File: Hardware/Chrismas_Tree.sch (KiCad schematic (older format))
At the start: 0 parts

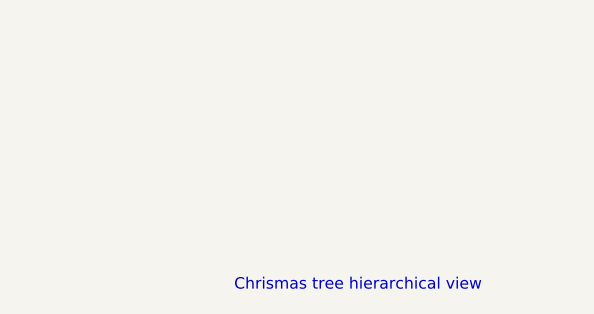
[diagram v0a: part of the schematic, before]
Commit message: Used standard schematic title blocks titles.
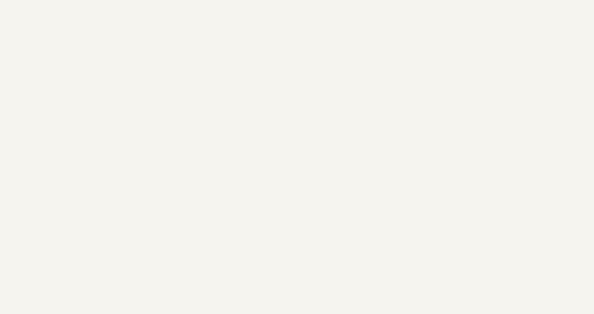
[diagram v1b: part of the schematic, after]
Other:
- note removed: "Chrismas tree hierarchical view"
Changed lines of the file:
@@
 EESchema Schematic File Version 4
-LIBS:Chrismas_Tree-cache
 EELAYER 30 0
 EELAYER END
@@
 encoding utf-8
 Sheet 1 3
-Title ""
+Title "Chrismas tree hierarchical view"
 Date ""
 Rev ""
-Comp ""
+Comp "Adrien RICCIARDI"
 Comment1 ""
 Comment2 ""
@@
 F1 "Tree_Shape.sch" 50
 $EndSheet
-Text Notes 7400 7500 0    50   ~ 0
-Chrismas tree hierarchical view
 $Sheet
 S 4600 3350 1250 1100

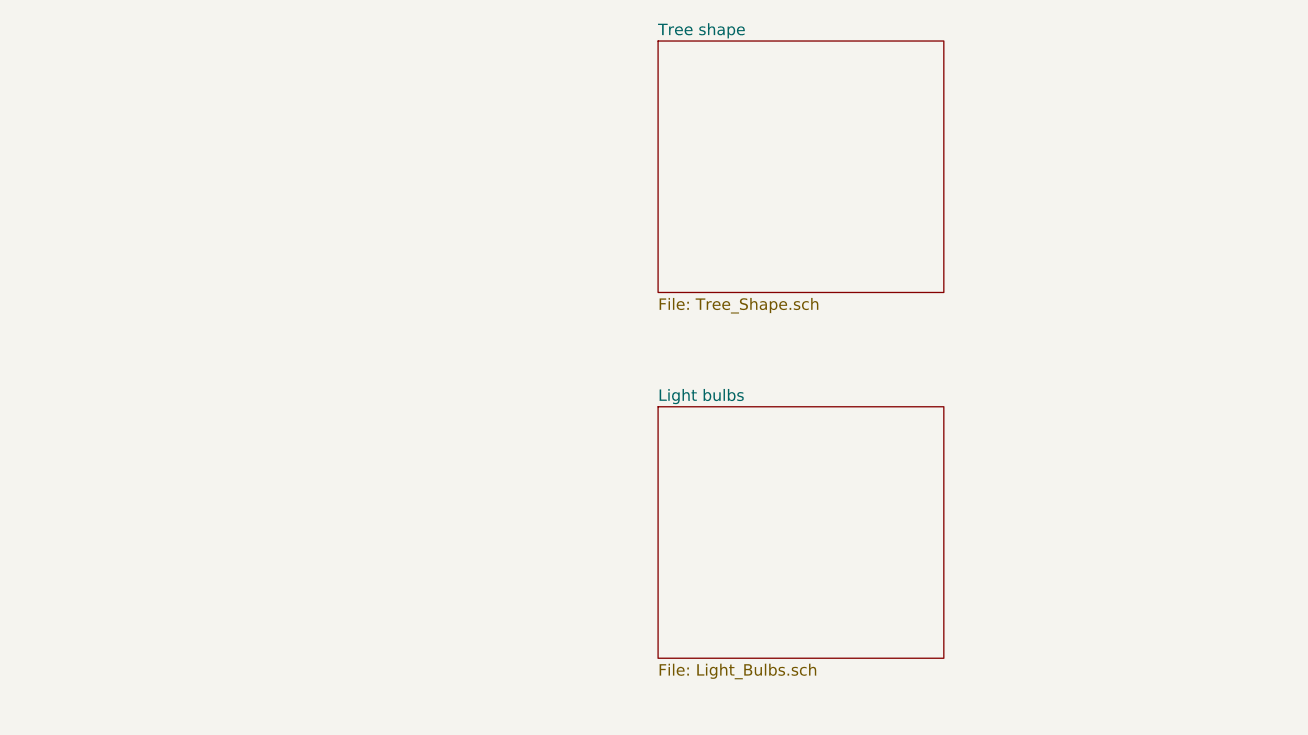
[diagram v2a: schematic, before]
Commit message: Added mounting holes to schematic.
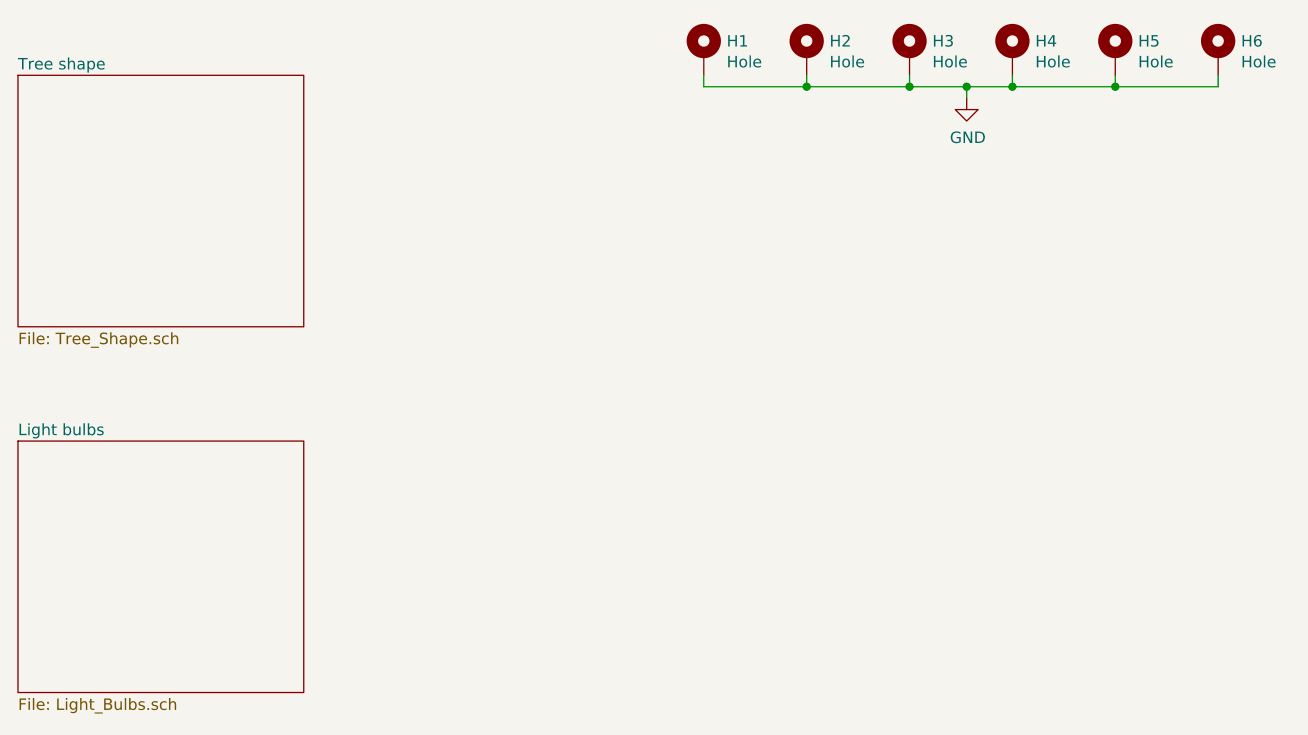
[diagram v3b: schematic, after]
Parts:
- added H1, H2, H3, H4, H5, H6: Hole, MountingHole:MountingHole_4.5mm_Pad, symbol Mechanical:MountingHole_Pad
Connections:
- new net GND: H1.1, H2.1, H3.1, H4.1, H5.1, H6.1
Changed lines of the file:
@@
 $EndDescr
 $Sheet
-S 4600 1750 1250 1100
+S 1800 1900 1250 1100
 U 5DE1DFF6
 F0 "Tree shape" 50
@@
 $EndSheet
 $Sheet
-S 4600 3350 1250 1100
+S 1800 3500 1250 1100
 U 5DE2A82E
 F0 "Light bulbs" 50
 F1 "Light_Bulbs.sch" 50
 $EndSheet
+$Comp
+L Mechanical:MountingHole_Pad H1
+U 1 1 5DE4B967
+P 4800 1800
+F 0 "H1" H 4900 1849 50  0000 L CNN
+F 1 "Hole" H 4900 1758 50  0000 L CNN
+F 2 "MountingHole:MountingHole_4.5mm_Pad" H 4800 1800 50  0001 C CNN
+F 3 "~" H 4800 1800 50  0001 C CNN
+	1    4800 1800
+	1    0    0    -1
+$EndComp
+$Comp
+L Mechanical:MountingHole_Pad H2
+U 1 1 5DE4DC82
+P 5250 1800
+F 0 "H2" H 5350 1849 50  0000 L CNN
+F 1 "Hole" H 5350 1758 50  0000 L CNN
+F 2 "MountingHole:MountingHole_4.5mm_Pad" H 5250 1800 50  0001 C CNN
+F 3 "~" H 5250 1800 50  0001 C CNN
+	1    5250 1800
+	1    0    0    -1
+$EndComp
+$Comp
+L Mechanical:MountingHole_Pad H3
+U 1 1 5DE4DF24
+P 5700 1800
+F 0 "H3" H 5800 1849 50  0000 L CNN
+F 1 "Hole" H 5800 1758 50  0000 L CNN
+F 2 "MountingHole:MountingHole_4.5mm_Pad" H 5700 1800 50  0001 C CNN
+F 3 "~" H 5700 1800 50  0001 C CNN
+	1    5700 1800
+	1    0    0    -1
+$EndComp
+$Comp
+L Mechanical:MountingHole_Pad H4
+U 1 1 5DE4E445
+P 6150 1800
+F 0 "H4" H 6250 1849 50  0000 L CNN
+F 1 "Hole" H 6250 1758 50  0000 L CNN
+F 2 "MountingHole:MountingHole_4.5mm_Pad" H 6150 1800 50  0001 C CNN
+F 3 "~" H 6150 1800 50  0001 C CNN
+	1    6150 1800
+	1    0    0    -1
+$EndComp
+$Comp
+L Mechanical:MountingHole_Pad H5
+U 1 1 5DE4E44F
+P 6600 1800
+F 0 "H5" H 6700 1849 50  0000 L CNN
+F 1 "Hole" H 6700 1758 50  0000 L CNN
+F 2 "MountingHole:MountingHole_4.5mm_Pad" H 6600 1800 50  0001 C CNN
+F 3 "~" H 6600 1800 50  0001 C CNN
+	1    6600 1800
+	1    0    0    -1
+$EndComp
+$Comp
+L Mechanical:MountingHole_Pad H6
+U 1 1 5DE4E459
+P 7050 1800
+F 0 "H6" H 7150 1849 50  0000 L CNN
+F 1 "Hole" H 7150 1758 50  0000 L CNN
+F 2 "MountingHole:MountingHole_4.5mm_Pad" H 7050 1800 50  0001 C CNN
+F 3 "~" H 7050 1800 50  0001 C CNN
+	1    7050 1800
+	1    0    0    -1
+$EndComp
+$Comp
+L power:GND #PWR0102
+U 1 1 5DE4EE07
+P 5950 2000
+F 0 "#PWR0102" H 5950 1750 50  0001 C CNN
+F 1 "GND" H 5955 1827 50  0000 C CNN
+F 2 "" H 5950 2000 50  0001 C CNN
+F 3 "" H 5950 2000 50  0001 C CNN
+	1    5950 2000
+	1    0    0    -1
+$EndComp
+Wire Wire Line
+	4800 1900 4800 1950
+Wire Wire Line
+	4800 1950 5250 1950
+Wire Wire Line
+	5250 1950 5250 1900
+Wire Wire Line
+	5250 1950 5700 1950
+Wire Wire Line
+	5700 1950 5700 1900
+Connection ~ 5250 1950
+Wire Wire Line
+	5700 1950 5950 1950
+Wire Wire Line
+	6150 1950 6150 1900
+Connection ~ 5700 1950
+Wire Wire Line
+	5950 1950 5950 2000
+Connection ~ 5950 1950
+Wire Wire Line
+	5950 1950 6150 1950
+Wire Wire Line
+	6150 1950 6600 1950
+Wire Wire Line
+	6600 1950 6600 1900
+Connection ~ 6150 1950
+Wire Wire Line
+	6600 1950 7050 1950
+Wire Wire Line
+	7050 1950 7050 1900
+Connection ~ 6600 1950
 $EndSCHEMATC

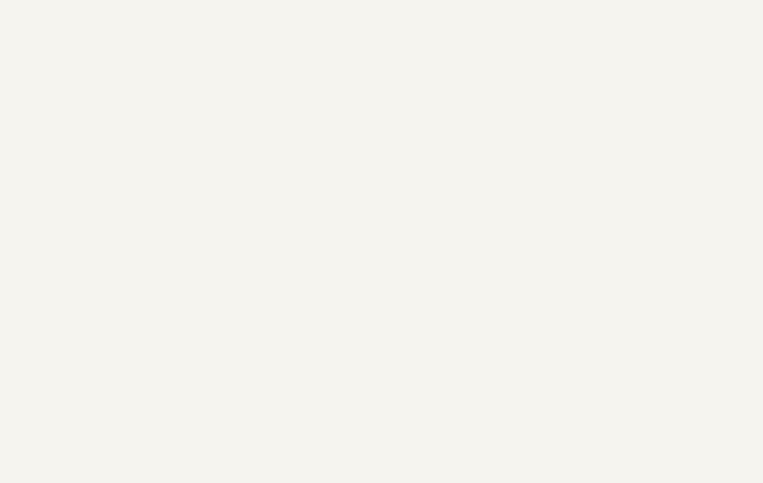
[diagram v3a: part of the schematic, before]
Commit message: Replaced USB micro B connector by a more robust USB B one.
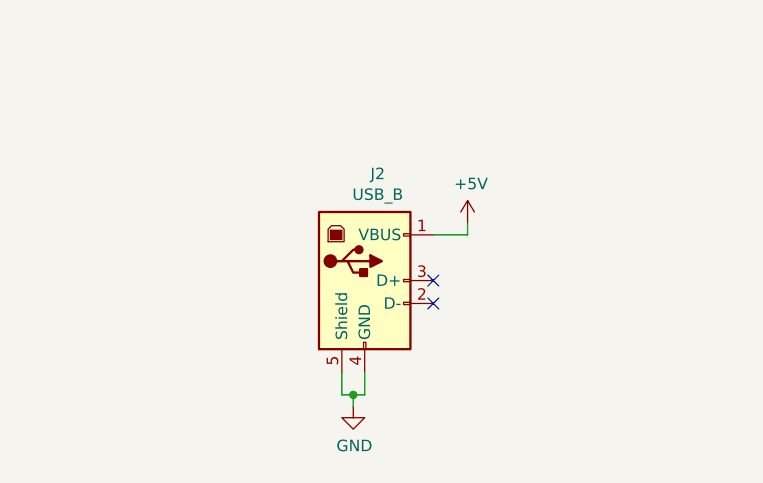
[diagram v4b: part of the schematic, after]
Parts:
- added J2: USB_B, Connector_USB:USB_B_OST_USB-B1HSxx_Horizontal, symbol Connector:USB_B
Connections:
- net GND: now also J2.4 (GND), J2.5 (Shield)
- new net +5V: J2.1 (VBUS)
- no-connect marks 0 -> 2
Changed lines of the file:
@@
 	7050 1950 7050 1900
 Connection ~ 6600 1950
+Wire Wire Line
+	5650 4400 5700 4400
+Wire Wire Line
+	5650 4450 5650 4400
+$Comp
+L power:GND #PWR?
+U 1 1 5DE42A6F
+P 5650 4450
+AR Path="/5DE2A82E/5DE42A6F" Ref="#PWR?"  Part="1"
+AR Path="/5DE42A6F" Ref="#PWR0118"  Part="1"
+F 0 "#PWR0118" H 5650 4200 50  0001 C CNN
+F 1 "GND" H 5655 4277 50  0000 C CNN
+F 2 "" H 5650 4450 50  0001 C CNN
+F 3 "" H 5650 4450 50  0001 C CNN
+	1    5650 4450
+	1    0    0    -1
+$EndComp
+Wire Wire Line
+	5700 4400 5700 4300
+Connection ~ 5650 4400
+Wire Wire Line
+	5600 4400 5650 4400
+Wire Wire Line
+	5600 4300 5600 4400
+Wire Wire Line
+	6150 3700 6150 3650
+Wire Wire Line
+	6000 3700 6150 3700
+$Comp
+L power:+5V #PWR?
+U 1 1 5DE42A7B
+P 6150 3650
+AR Path="/5DE2A82E/5DE42A7B" Ref="#PWR?"  Part="1"
+AR Path="/5DE42A7B" Ref="#PWR0119"  Part="1"
+F 0 "#PWR0119" H 6150 3500 50  0001 C CNN
+F 1 "+5V" H 6165 3823 50  0000 C CNN
+F 2 "" H 6150 3650 50  0001 C CNN
+F 3 "" H 6150 3650 50  0001 C CNN
+	1    6150 3650
+	1    0    0    -1
+$EndComp
+$Comp
+L Connector:USB_B J2
+U 1 1 5DE42DBE
+P 5700 3900
+F 0 "J2" H 5757 4367 50  0000 C CNN
+F 1 "USB_B" H 5757 4276 50  0000 C CNN
+F 2 "Connector_USB:USB_B_OST_USB-B1HSxx_Horizontal" H 5850 3850 50  0001 C CNN
+F 3 " ~" H 5850 3850 50  0001 C CNN
+	1    5700 3900
+	1    0    0    -1
+$EndComp
+NoConn ~ 6000 3900
+NoConn ~ 6000 4000
 $EndSCHEMATC

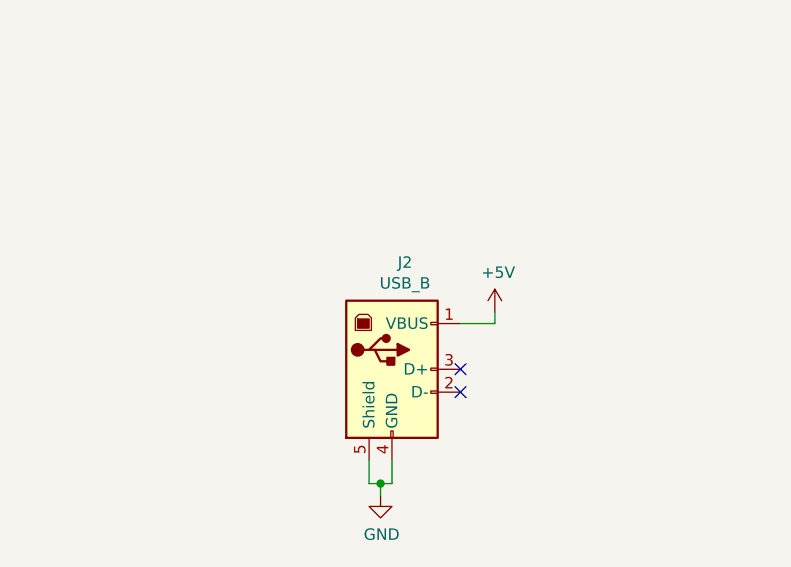
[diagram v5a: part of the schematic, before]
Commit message: Updated USB connector symbol reference in schematic to conform to KiCad 5.1.10.
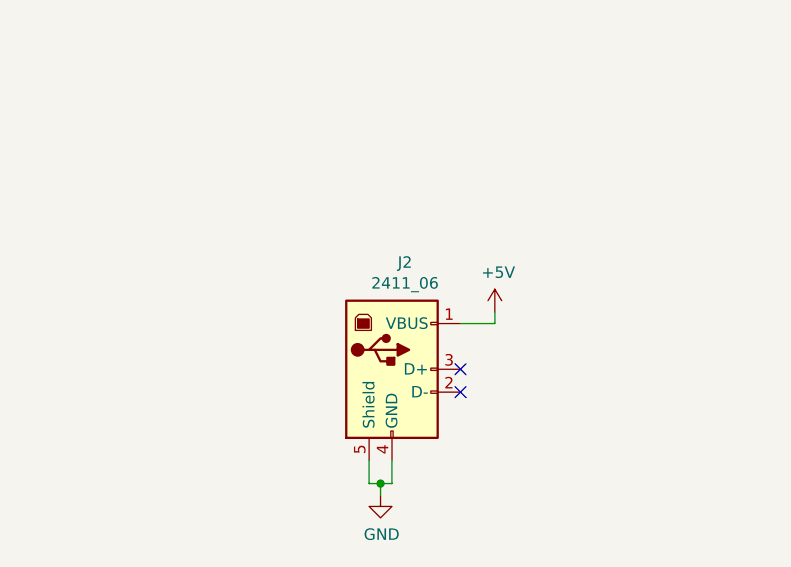
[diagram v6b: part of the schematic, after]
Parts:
- J2: value USB_B -> 2411_06; Manufacturer (none) -> Lumberg
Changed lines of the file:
@@
 P 5700 3900
 F 0 "J2" H 5757 4367 50  0000 C CNN
-F 1 "USB_B" H 5757 4276 50  0000 C CNN
+F 1 "2411_06" H 5757 4276 50  0000 C CNN
 F 2 "Connector_USB:USB_B_OST_USB-B1HSxx_Horizontal" H 5850 3850 50  0001 C CNN
 F 3 " ~" H 5850 3850 50  0001 C CNN
+F 4 "Lumberg" H 5700 3900 50  0001 C CNN "Manufacturer"
 	1    5700 3900
 	1    0    0    -1

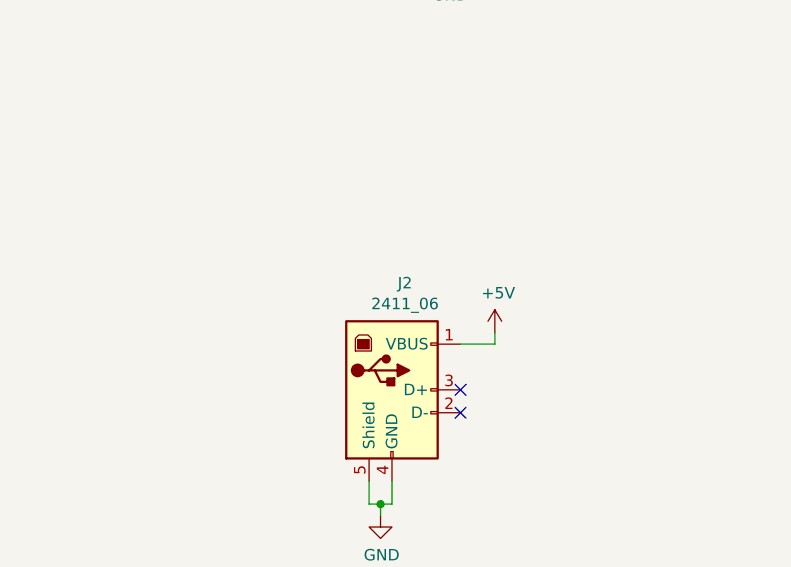
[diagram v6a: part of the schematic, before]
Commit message: Updated bill of materials data on schematic to improve generated bill of materials.
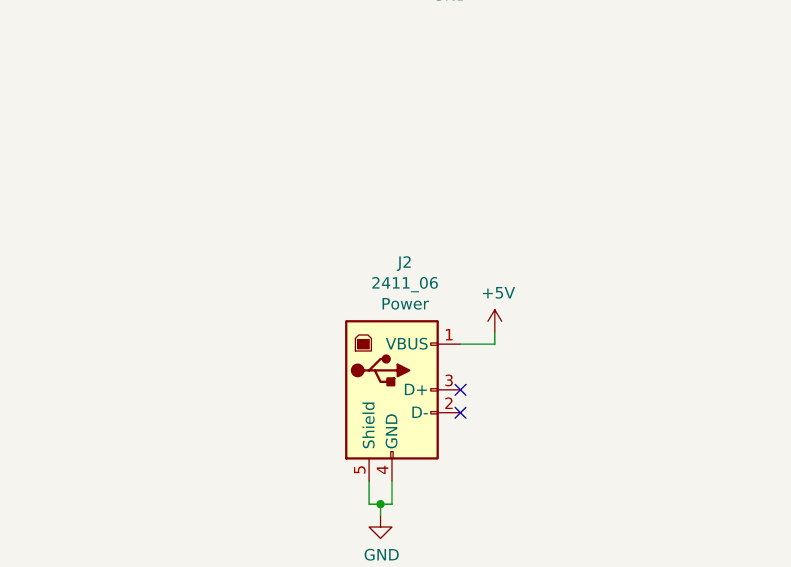
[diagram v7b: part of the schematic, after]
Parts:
- J2: Description (none) -> Power
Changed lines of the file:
@@
 U 1 1 5DE42DBE
 P 5700 3900
-F 0 "J2" H 5757 4367 50  0000 C CNN
-F 1 "2411_06" H 5757 4276 50  0000 C CNN
+F 0 "J2" H 5757 4457 50  0000 C CNN
+F 1 "2411_06" H 5757 4366 50  0000 C CNN
 F 2 "Connector_USB:USB_B_OST_USB-B1HSxx_Horizontal" H 5850 3850 50  0001 C CNN
 F 3 " ~" H 5850 3850 50  0001 C CNN
 F 4 "Lumberg" H 5700 3900 50  0001 C CNN "Manufacturer"
+F 5 "Power" H 5757 4275 50  0000 C CNN "Description"
 	1    5700 3900
 	1    0    0    -1

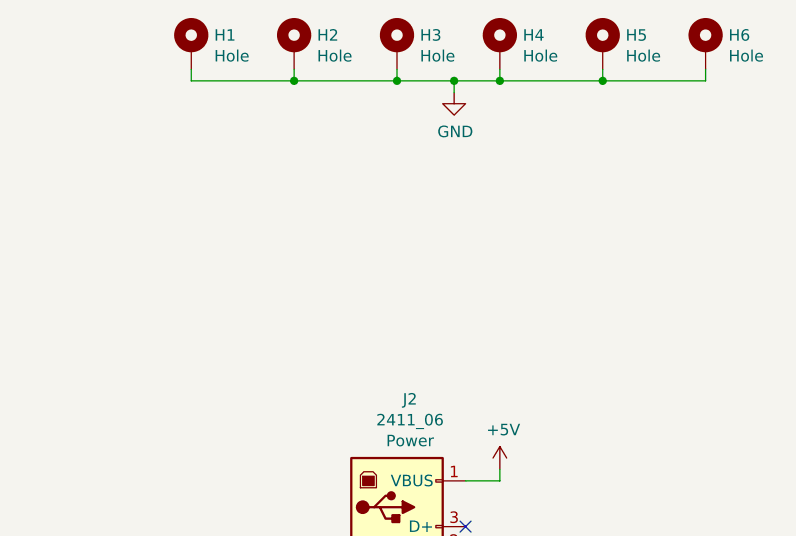
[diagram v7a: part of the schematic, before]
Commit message: Added fiducials to PCB.
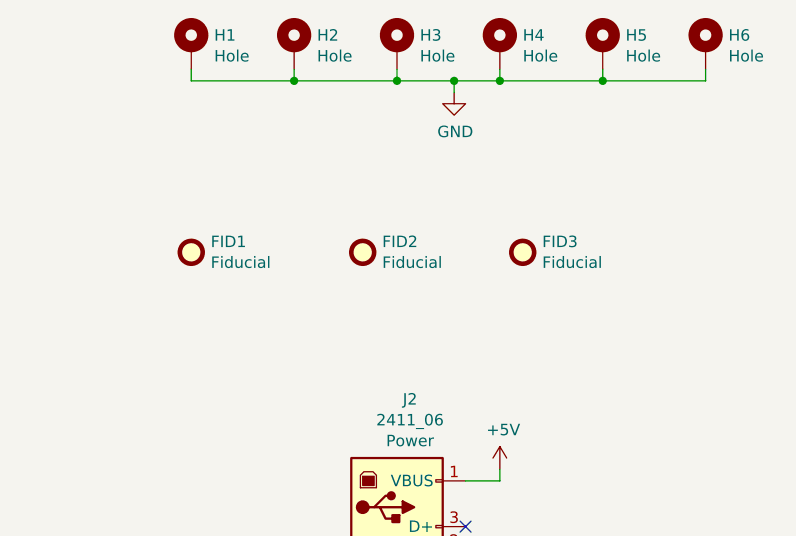
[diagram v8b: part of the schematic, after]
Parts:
- added FID1, FID2, FID3: Fiducial, Fiducial:Fiducial_1.5mm_Mask3mm, symbol Mechanical:Fiducial
- H1, H2, H3, H4, H5, H6: Populate (none) -> DNP
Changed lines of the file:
@@
 F 2 "MountingHole:MountingHole_4.5mm_Pad" H 4800 1800 50  0001 C CNN
 F 3 "~" H 4800 1800 50  0001 C CNN
+F 4 "DNP" H 4800 1800 50  0001 C CNN "Populate"
 	1    4800 1800
 	1    0    0    -1
@@
 F 2 "MountingHole:MountingHole_4.5mm_Pad" H 5250 1800 50  0001 C CNN
 F 3 "~" H 5250 1800 50  0001 C CNN
+F 4 "DNP" H 5250 1800 50  0001 C CNN "Populate"
 	1    5250 1800
 	1    0    0    -1
@@
 F 2 "MountingHole:MountingHole_4.5mm_Pad" H 5700 1800 50  0001 C CNN
 F 3 "~" H 5700 1800 50  0001 C CNN
+F 4 "DNP" H 5700 1800 50  0001 C CNN "Populate"
 	1    5700 1800
 	1    0    0    -1
@@
 F 2 "MountingHole:MountingHole_4.5mm_Pad" H 6150 1800 50  0001 C CNN
 F 3 "~" H 6150 1800 50  0001 C CNN
+F 4 "DNP" H 6150 1800 50  0001 C CNN "Populate"
 	1    6150 1800
 	1    0    0    -1
@@
 F 2 "MountingHole:MountingHole_4.5mm_Pad" H 6600 1800 50  0001 C CNN
 F 3 "~" H 6600 1800 50  0001 C CNN
+F 4 "DNP" H 6600 1800 50  0001 C CNN "Populate"
 	1    6600 1800
 	1    0    0    -1
@@
 F 2 "MountingHole:MountingHole_4.5mm_Pad" H 7050 1800 50  0001 C CNN
 F 3 "~" H 7050 1800 50  0001 C CNN
+F 4 "DNP" H 7050 1800 50  0001 C CNN "Populate"
 	1    7050 1800
 	1    0    0    -1
@@
 NoConn ~ 6000 3900
 NoConn ~ 6000 4000
+$Comp
+L Mechanical:Fiducial FID1
+U 1 1 619FF64A
+P 4800 2700
+F 0 "FID1" H 4885 2746 50  0000 L CNN
+F 1 "Fiducial" H 4885 2655 50  0000 L CNN
+F 2 "Fiducial:Fiducial_1.5mm_Mask3mm" H 4800 2700 50  0001 C CNN
+F 3 "~" H 4800 2700 50  0001 C CNN
+F 4 "DNP" H 4800 2700 50  0001 C CNN "Populate"
+	1    4800 2700
+	1    0    0    -1
+$EndComp
+$Comp
+L Mechanical:Fiducial FID2
+U 1 1 61A00A24
+P 5550 2700
+F 0 "FID2" H 5635 2746 50  0000 L CNN
+F 1 "Fiducial" H 5635 2655 50  0000 L CNN
+F 2 "Fiducial:Fiducial_1.5mm_Mask3mm" H 5550 2700 50  0001 C CNN
+F 3 "~" H 5550 2700 50  0001 C CNN
+F 4 "DNP" H 5550 2700 50  0001 C CNN "Populate"
+	1    5550 2700
+	1    0    0    -1
+$EndComp
+$Comp
+L Mechanical:Fiducial FID3
+U 1 1 61A00D88
+P 6250 2700
+F 0 "FID3" H 6335 2746 50  0000 L CNN
+F 1 "Fiducial" H 6335 2655 50  0000 L CNN
+F 2 "Fiducial:Fiducial_1.5mm_Mask3mm" H 6250 2700 50  0001 C CNN
+F 3 "~" H 6250 2700 50  0001 C CNN
+F 4 "DNP" H 6250 2700 50  0001 C CNN "Populate"
+	1    6250 2700
+	1    0    0    -1
+$EndComp
 $EndSCHEMATC
